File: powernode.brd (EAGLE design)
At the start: 100 x 50 mm, 29 parts, among them J1 ATX24RH, X1 5566-4, X2 5566-6

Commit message: working on powernode.
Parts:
- removed J1: ATX24RH, SparkFun-Connectors:ATX24_RIGHT_ANGLE
- added X3: 5566-24, con-molex:5566-24
- moved C2 8.25 mm to (56.8, 25.4)
- moved U$1 6.00 mm to (47.8, 26.2)
- moved X1 4.00 mm to (14.0, 8.00)
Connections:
- net +12V: now also X3.10, X3.11; no longer J1.10, J1.11
- net +3V3: now also X3.1, X3.12, X3.13, X3.2; no longer J1.1, J1.12, J1.13, J1.2
- net +5V: now also X3.21, X3.22, X3.23, X3.4, X3.6; no longer J1.21, J1.22, J1.23, J1.4, J1.6
- net +5V/2: now also X3.9; no longer J1.9
- net -12V: now also X3.14; no longer J1.14
- net GND: now also X3.15, X3.17, X3.18, X3.19, X3.24, X3.3, X3.5, X3.7; no longer J1.15, J1.17, J1.18, J1.19, J1.24, J1.3, J1.5, J1.7
- net PS_ON: now also X3.16; no longer J1.16
- net PWR_OK: now also X3.8; no longer J1.8

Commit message: Working on powernone.
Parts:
- removed C3: 100 nF, rcl:C0805
- removed JP5, JP6: (no value), SparkFun-Connectors:SCREWTERMINAL-5MM-3
- removed S1: (no value), SparkFun:SWITCH-SPDT
- added BLUETOOTH: (no value), SparkFun-Connectors:1X06_NO_SILK
- added ETHERNET: (no value), con-lsta:FE06-2
- added LED1: (no value), led:LED3MM
- added R1: (no value), rcl:R0805
- added RN1: 10k, resistor-dil:0603-ARC
- added SWITCH: (no value), SparkFun-Connectors:1X03
- C1: value 100 nF -> 10 uF; device rcl:C0805 -> rcl:C1206
- U$1: device SparkFun-Boards:ARDUINO_PRO_MINI -> SparkFun-Boards-with-arduino-pro-mini-without-connection-pins:ARDUINO_PRO_MINI
- moved JP2 84.2 mm to (13.0, 45.0), turned to 0 degrees
- moved JP3 77.1 mm to (76.0, 45.0), turned to 0 degrees
- moved JP1 76.3 mm to (5.00, 17.0), turned to 90 degrees
- moved C7 63.7 mm to (16.9, 20.9), turned to 180 degrees
- moved C5 55.7 mm to (84.1, 18.7), turned to 0 degrees
- moved JP4 39.4 mm to (94.0, 27.0), turned to 270 degrees
- moved C2 23.0 mm to (39.0, 40.0), turned to 0 degrees
- moved C4 16.5 mm to (17.3, 18.2), turned to 180 degrees
- moved C8 13.4 mm to (84.7, 25.2)
- moved C1 12.1 mm to (39.0, 37.0), turned to 0 degrees
- moved C6 7.97 mm to (85.1, 22.0), turned to 0 degrees
- moved C9 5.83 mm to (16.5, 25.3)
- moved PIR 5.10 mm to (47.0, 46.0), turned to 0 degrees
- moved U$1 0.68 mm to (47.2, 25.8), turned to 90 degrees
- renumbered JP10 to LEDS4, JP7 to LEDS1, JP8 to LEDS2, JP9 to LEDS3
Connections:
- new net BLUETOOTH_KEY: BLUETOOTH.6
- new net BLUETOOTH_RXD: RN1.8, U$1.1
- new net BLUETOOTH_STATE: BLUETOOTH.1
- new net BLUETOOTH_TXD: BLUETOOTH.3, U$1.2
- new net DATA_BUS: JP1.3, JP2.3, JP3.3, JP4.3, U$1.17
- new net ETHERNET_3_3V: ETHERNET.1
- new net ETHERNET_CLK: ETHERNET.10
- new net ETHERNET_CS: ETHERNET.4, U$1.11
- new net ETHERNET_INT: ETHERNET.9
- new net ETHERNET_SCK: ETHERNET.5, U$1.16
- new net ETHERNET_SI: ETHERNET.6, U$1.14
- new net ETHERNET_SO: ETHERNET.7, U$1.15
- new net ETHERNET_WAKE_ON_LAN: ETHERNET.8
- new net LEDSTRIP1: LEDS1.2
- new net LEDSTRIP2: LEDS2.2
- new net LEDSTRIP3: LEDS3.2
- new net LEDSTRIP4: LEDS4.2
- new net N$1: U$1.A6
- new net N$10: U$1.20
- new net N$11: U$1.5
- new net N$12: U$1.6
- new net N$13: U$1.7
- new net N$14: U$1.8
- new net N$15: U$1.9
- new net N$16: U$1.10
- new net N$18: U$1.12
- new net N$19: U$1.A4
- new net N$2: U$1.A7
- new net N$20: U$1.A5
- new net N$21: BLUETOOTH.2, RN1.1, RN1.2
- new net N$22: U$1.24
- new net N$3: U$1.13
- new net N$4: RN1.6, RN1.7
- new net N$5: RN1.4, SWITCH.2
- new net N$6: LED1.A, R1.1
- new net N$8: U$1.18
- new net N$9: U$1.19
- new net POWER_SWITCH: RN1.5
- new net RESET: ETHERNET.3, U$1.3
- net +12V: now also C4.1, C5.1, C6.1, C7.1, C8.+, C9.+, JP1.1, JP2.1, JP3.1, JP4.1, LEDS1.1, LEDS2.1, LEDS3.1, LEDS4.1, R1.2
- net +5V: no longer C1.1, C2.1, C3.1, C4.1, C5.1, C6.1, C7.1, C8.+, C9.+
- net +5V/2: now also BLUETOOTH.5, C1.1, C2.1, ETHERNET.11, SWITCH.3
- net GND: now also BLUETOOTH.4, ETHERNET.12, ETHERNET.2, JP1.2, JP2.2, JP3.2, JP4.2, LED1.K, LEDS1.3, LEDS2.3, LEDS3.3, LEDS4.3, RN1.3, SWITCH.1; no longer C3.2, S1.3
- net PS_ON: no longer S1.2

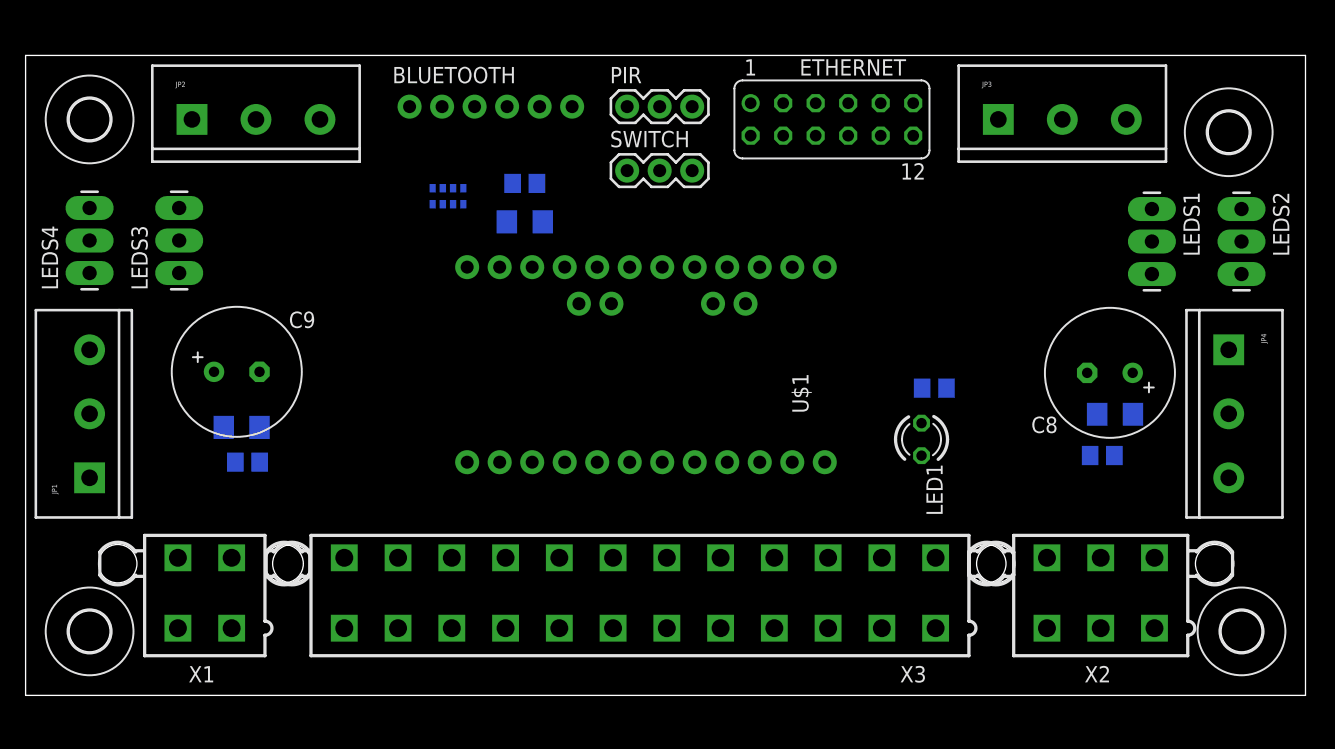
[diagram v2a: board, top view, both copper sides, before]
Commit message: Working on power / control node.
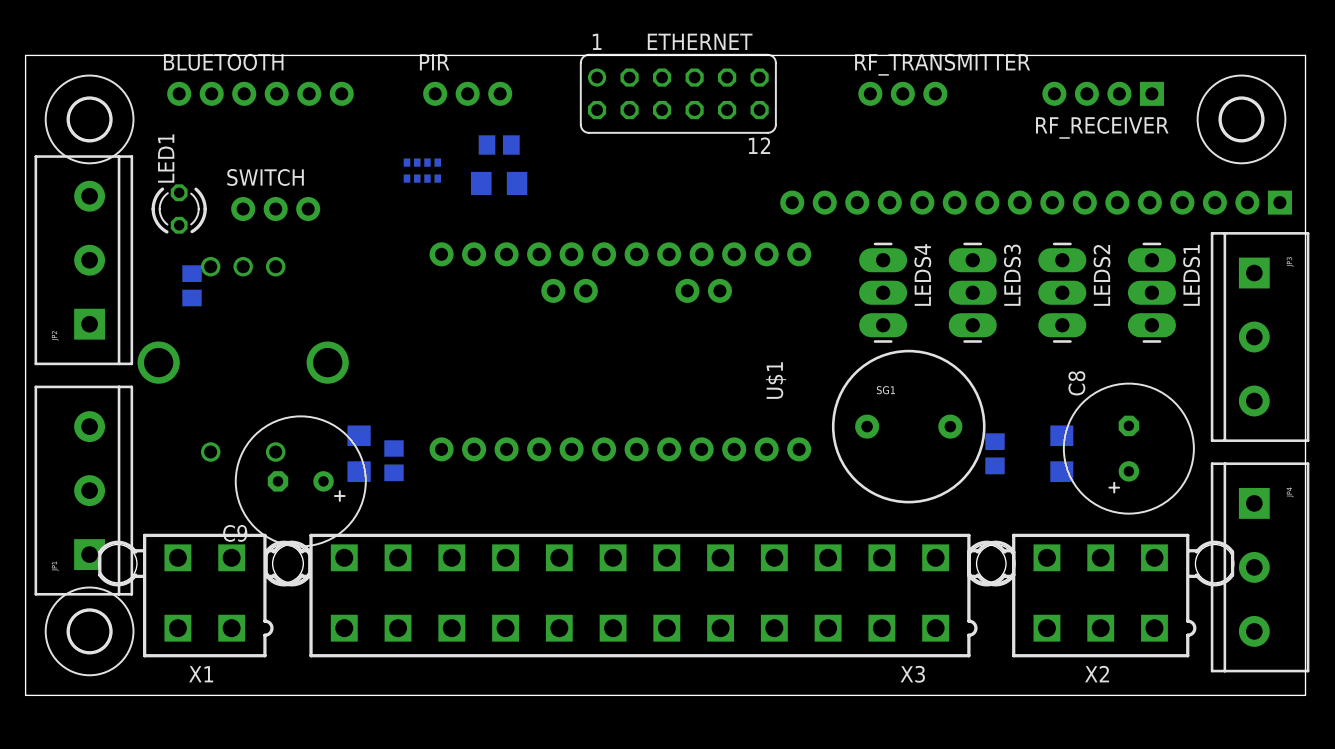
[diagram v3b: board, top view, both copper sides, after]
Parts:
- removed H4: MOUNT-HOLE3.2, holes:3,2
- added RF_RECEIVER: (no value), SparkFun-Connectors:1X04_NO_SILK
- added RF_TRANSMITTER: (no value), SparkFun-Connectors:1X03_NO_SILK
- added SG1: BUZZERPTH-KIT, SparkFun-Electromechanical:BUZZER-12MM-KIT
- added SW1: ROTARTY_ENCODER, SparkFun-Electromechanical:ROTARY_ENC_PLAIN
- added U1: LCD-16X2NOHOLES, SparkFun:LCD-16X2_NOHOLES
- PIR, SWITCH: device SparkFun-Connectors:1X03 -> SparkFun-Connectors:1X03_NO_SILK
- moved LEDS3 62.0 mm to (74.0, 34.0), turned to 270 degrees
- moved LEDS4 62.0 mm to (67.0, 34.0), turned to 270 degrees
- moved LED1 60.7 mm to (12.0, 38.0), turned to 90 degrees
- moved R1 58.5 mm to (13.0, 32.0), turned to 270 degrees
- moved SWITCH 30.1 mm to (17.0, 38.0)
- moved JP3 23.3 mm to (96.0, 33.0), turned to 270 degrees
- moved BLUETOOTH 18.0 mm to (12.0, 47.0)
- moved JP2 17.9 mm to (5.00, 29.0), turned to 90 degrees
- moved PIR 15.0 mm to (32.0, 47.0)
- moved LEDS2 14.6 mm to (81.0, 34.0)
- moved ETHERNET 12.2 mm to (51.0, 47.0)
- moved JP4 12.2 mm to (96.0, 15.0)
- moved C4 11.4 mm to (28.8, 18.3), turned to 90 degrees
- moved C9 9.91 mm to (21.5, 16.7), turned to 180 degrees
- moved C7 9.41 mm to (26.1, 18.9), turned to 90 degrees
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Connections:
- new net A: U1.15
- new net K: U1.16
- new net RF_DATA_IN: RF_RECEIVER.2, RF_RECEIVER.3
- new net RF_DATA_OUT: RF_TRANSMITTER.1
- new net VDD: U1.2
- new net VSS: U1.1
- net +5V/2: now also RF_RECEIVER.1, RF_TRANSMITTER.2
- net GND: now also RF_RECEIVER.4, RF_TRANSMITTER.3

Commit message: Work on powernode.
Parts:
- removed H1, H2, H3: MOUNT-HOLE3.2, holes:3,2
- removed LED1: (no value), led:LED3MM
- removed LEDS3, LEDS4: (no value), SparkFun-Connectors:1X03_LONGPADS
- removed SWITCH: (no value), SparkFun-Connectors:1X03_NO_SILK
- added C10: 100 uF, rcl:E3,5-10
- added C11, C3: 100 nF, rcl:C0805
- added CLOCK,TEMP,I2C: (no value), SparkFun:1X05
- added IC1: 74HC595D, 74xx-eu:SO16
- added POWER_SWITCH: KNC1-101-2P, knc1-101-switch:KNC1-101-2P
- added R2, R4: (no value), rcl:R0805
- added R3: 10k, resistor:RTRIM3296W
- added R5: (4k), rcl:R0805
- added STATUS_LED: (no value), led:DUOLED-C-5MM
- R1: value (none) -> (4k)
- X1: device con-molex:5566-4 -> con-molex--with-atx-connectors-without-side-screws:5566-4
- X2: device con-molex:5566-6 -> con-molex--with-atx-connectors-without-side-screws:5566-6
- X3: device con-molex:5566-24 -> con-molex--with-atx-connectors-without-side-screws:5566-24
- moved PIR 41.0 mm to (73.0, 48.0)
- moved R1 38.9 mm to (50.0, 44.0), flipped to the top
- moved C2 17.7 mm to (42.0, 26.0), turned to 270 degrees
- moved C1 17.2 mm to (47.0, 26.0), turned to 270 degrees
- moved C9 15.7 mm to (14.5, 30.7)
- moved RN1 15.3 mm to (16.0, 44.0), flipped to the top
- moved C4 14.1 mm to (14.7, 18.8), flipped to the top, turned to 0 degrees
- moved ETHERNET 14.0 mm to (37.0, 47.0)
- moved C5 11.9 mm to (86.1, 24.7), turned to 0 degrees
- moved C7 11.7 mm to (15.1, 23.1), flipped to the top, turned to 0 degrees
- moved LEDS1 8.25 mm to (80.0, 36.0)
- moved LEDS2 6.32 mm to (87.0, 36.0)
- moved JP4 5.39 mm to (94.0, 20.0)
- moved C6 5.18 mm to (85.1, 22.0), turned to 0 degrees
- moved SW1 5.10 mm to (18.0, 21.0), turned to 180 degrees
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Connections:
- removed net A: U1.15
- removed net K: U1.16
- removed net LEDSTRIP3: LEDS3.2
- removed net LEDSTRIP4: LEDS4.2
- removed net N$12: U$1.6
- removed net N$13: U$1.7
- removed net N$14: U$1.8
- removed net N$15: U$1.9
- removed net N$16: U$1.10
- removed net N$18: U$1.12
- removed net N$19: U$1.A4
- removed net N$20: U$1.A5
- removed net N$22: U$1.24
- removed net N$6: LED1.A, R1.1
- removed net VDD: U1.2
- removed net VSS: U1.1
- new net BUZZER: C11.2, IC1.15, SG1.-
- new net ERROR_LED: IC1.7, R4.2
- new net LCD_BACKLIGHT: IC1.1, U1.16
- new net LCD_CLOCK: IC1.11, U$1.12
- new net LCD_DATA: IC1.14, U$1.A7
- new net LCD_ENABLE: IC1.12, U$1.13, U1.6
- new net N$7: IC1.4, U1.12
- new net SCL: CLOCK,TEMP,I2C.4, R1.2, U$1.A5
- new net SDA: CLOCK,TEMP,I2C.3, R5.2, U$1.A4
- new net TEMPERATURE_DS: CLOCK,TEMP,I2C.5
- new net TURN_WHEEL_A: SW1.A, U$1.5
- new net TURN_WHEEL_B: SW1.B, U$1.6
- new net TURN_WHEEL_CLICK: SW1.SW+, U$1.7
- net +12V: now also R2.2; no longer LEDS3.1, LEDS4.1, R1.2
- net +5V/2: now also C10.+, C11.1, C3.1, CLOCK,TEMP,I2C.2, IC1.10, IC1.16, R1.1, R3.3, R5.1, SG1.+, U1.15, U1.2; no longer SWITCH.3
- net GND: now also C10.-, C3.2, CLOCK,TEMP,I2C.1, IC1.13, IC1.8, POWER_SWITCH.P$1, R3.1, STATUS_LED.C, SW1.C, SW1.SW-, U1.1, U1.5; no longer LED1.K, LEDS3.3, LEDS4.3, SWITCH.1
- net LEDSTRIP1: now also U$1.9
- net LEDSTRIP2: now also U$1.10
- net N$1: now also IC1.3, U1.11; no longer U$1.A6
- net N$10: now also U1.3; no longer U$1.20
- net N$11: now also R4.1, STATUS_LED.AR; no longer U$1.5
- net N$2: now also IC1.2, U1.4; no longer U$1.A7
- net N$3: now also POWER_SWITCH.P$2, RN1.4; no longer U$1.13
- net N$5: now also R2.1, STATUS_LED.AX; no longer RN1.4, SWITCH.2
- net N$8: now also IC1.5, U1.13; no longer U$1.18
- net N$9: now also IC1.6, U1.14; no longer U$1.19
- net POWER_SWITCH: now also U$1.8
- net PROXIMITY: now also U$1.20
- net PS_ON: now also U$1.A6
- net RF_DATA_IN: now also U$1.18
- net RF_DATA_OUT: now also U$1.19
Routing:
- added copper zone on layer 1, net +12V
- added copper zone on layer 16, net GND
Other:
- outline, holes or cut-outs redrawn

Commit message: Working on powernode layout.
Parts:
- removed C3: 100 nF, rcl:C0805
- removed RN1: 10k, resistor-dil:0603-ARC
- added C12: 100 nF, rcl:C0805
- added C13: 10 uF, rcl:C1206
- added R6: 4.7k, rcl:R0805
- added R7: 1k, rcl:R0805
- added R8: 2k, rcl:R0805
- C10, C8, C9: device rcl:E3,5-10 -> rcl:E2,5-6
- C11: value 100 nF -> 100 uF; device rcl:C0805 -> rcl:E2,5-6
- moved C11 12.0 mm to (80.5, 18.5), flipped to the top
- moved C4 5.59 mm to (19.7, 21.3)
- moved R1 5.52 mm to (55.5, 44.5), turned to 180 degrees
- moved C7 4.61 mm to (19.6, 24.1)
- moved C8 4.31 mm to (85.5, 21.5)
- moved R4 4.12 mm to (25.0, 39.0), turned to 270 degrees
- moved SG1 3.61 mm to (72.0, 20.0)
- moved C10 3.54 mm to (80.5, 24.5)
- moved IC1 2.50 mm to (68.0, 32.5)
- moved C9 2.21 mm to (12.5, 29.8), turned to 0 degrees
- moved R5 2.06 mm to (51.0, 44.5), turned to 0 degrees
- moved LEDS1 0.50 mm to (80.0, 35.5)
- moved LEDS2 0.50 mm to (87.0, 35.5)
- flipped STATUS_LED to the bottom
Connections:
- removed net N$3: POWER_SWITCH.P$2, RN1.4
- removed net N$4: RN1.6, RN1.7
- net +5V: now also BLUETOOTH.5, C11.+, C12.1, C13.1, ETHERNET.11, R3.3, R6.2, RF_RECEIVER.1, RF_TRANSMITTER.2, SG1.+, U1.15, U1.2
- net +5V/2: no longer BLUETOOTH.5, C11.1, C3.1, ETHERNET.11, R3.3, RF_RECEIVER.1, RF_TRANSMITTER.2, SG1.+, U1.15, U1.2
- net BLUETOOTH_RXD: now also R7.2; no longer RN1.8
- net BUZZER: no longer C11.2
- net DATA_BUS: now also R6.1
- net GND: now also C11.-, C12.2, C13.2, R8.1; no longer C3.2, RN1.3
- net N$21: now also R7.1, R8.2; no longer RN1.1, RN1.2
- net POWER_SWITCH: now also POWER_SWITCH.P$2; no longer RN1.5
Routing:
- net +5V/2: track 0.00 -> 90.3 mm, vias 0 -> 1
- net +5V: track 0.00 -> 68.1 mm, vias 0 -> 1
- net LCD_ENABLE: track 0.00 -> 35.8 mm, vias 0 -> 1
- net PS_ON: track 0.00 -> 34.2 mm, vias 0 -> 3
- net N$2: track 0.00 -> 23.5 mm
- net LCD_BACKLIGHT: track 0.00 -> 18.6 mm, vias 0 -> 1
- net N$1: track 0.00 -> 7.04 mm
- net N$7: track 0.00 -> 6.52 mm
- net N$8: track 0.00 -> 6.00 mm
- net N$9: track 0.00 -> 4.91 mm
- added copper zone on layer 1, net +5V
